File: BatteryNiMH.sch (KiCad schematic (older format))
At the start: 0 parts

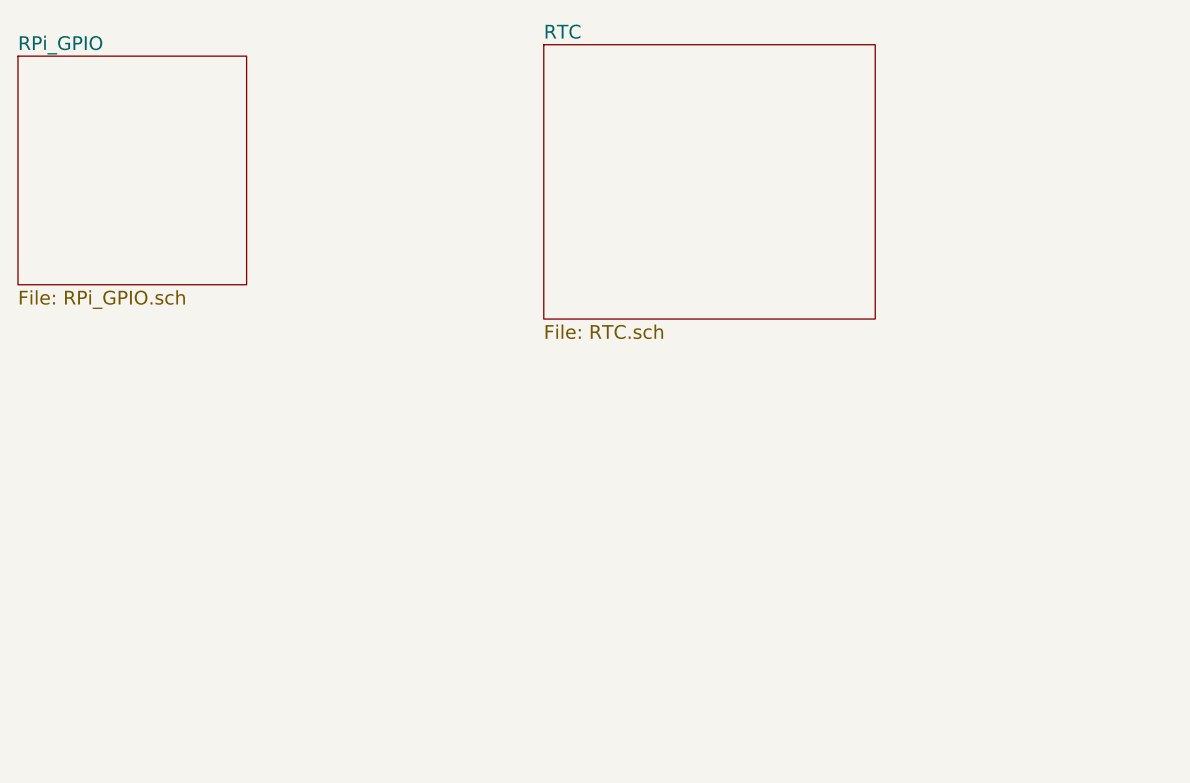
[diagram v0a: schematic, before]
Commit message: added power and nimh charge IC TODO charge circuit
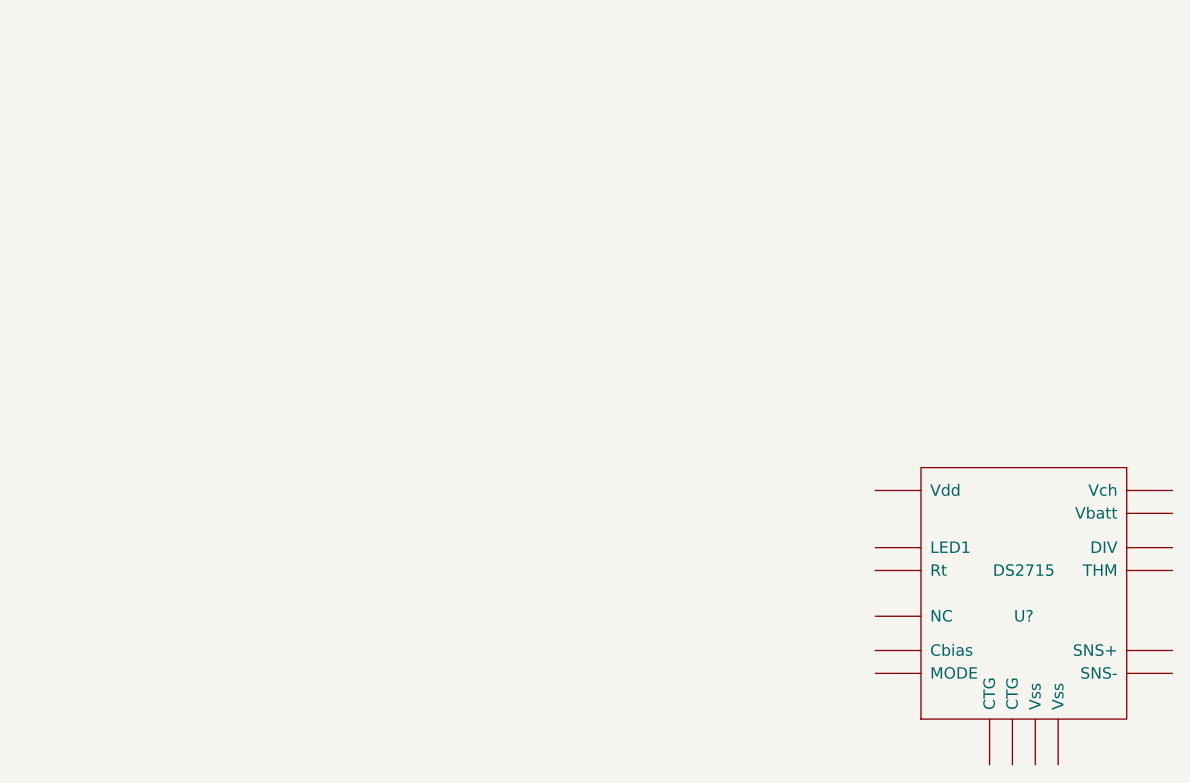
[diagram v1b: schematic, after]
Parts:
- added U?: DS2715, MODULE, symbol DS2715
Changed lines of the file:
@@
 LIBS:maxim
 LIBS:Ben
+LIBS:DS2715
 LIBS:RPi_RTC_RS232-cache
 EELAYER 25 0
@@
 $Descr A4 11693 8268
 encoding utf-8
-Sheet 1 3
+Sheet 6 6
 Title ""
 Date ""
@@
 Comment4 ""
 $EndDescr
-$Sheet
-S 1400 1400 1000 1000
-U 5515D395
-F0 "RPi_GPIO" 60
-F1 "RPi_GPIO.sch" 60
-$EndSheet
-$Sheet
-S 3700 1350 1450 1200
-U 5559D4CA
-F0 "RTC" 60
-F1 "RTC.sch" 60
-$EndSheet
+$Comp
+L DS2715 U?
+U 1 1 555CBA52
+P 5800 3750
+F 0 "U?" H 5800 3650 50  0000 C CNN
+F 1 "DS2715" H 5800 3850 50  0000 C CNN
+F 2 "MODULE" H 5800 3750 50  0001 C CNN
+F 3 "DOCUMENTATION" H 5800 3750 50  0001 C CNN
+	1    5800 3750
+	1    0    0    -1
+$EndComp
 $EndSCHEMATC
